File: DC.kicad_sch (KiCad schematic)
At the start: 39 parts, among them U6 MCP2551-I-P, U7 NUCLEO-F302R8

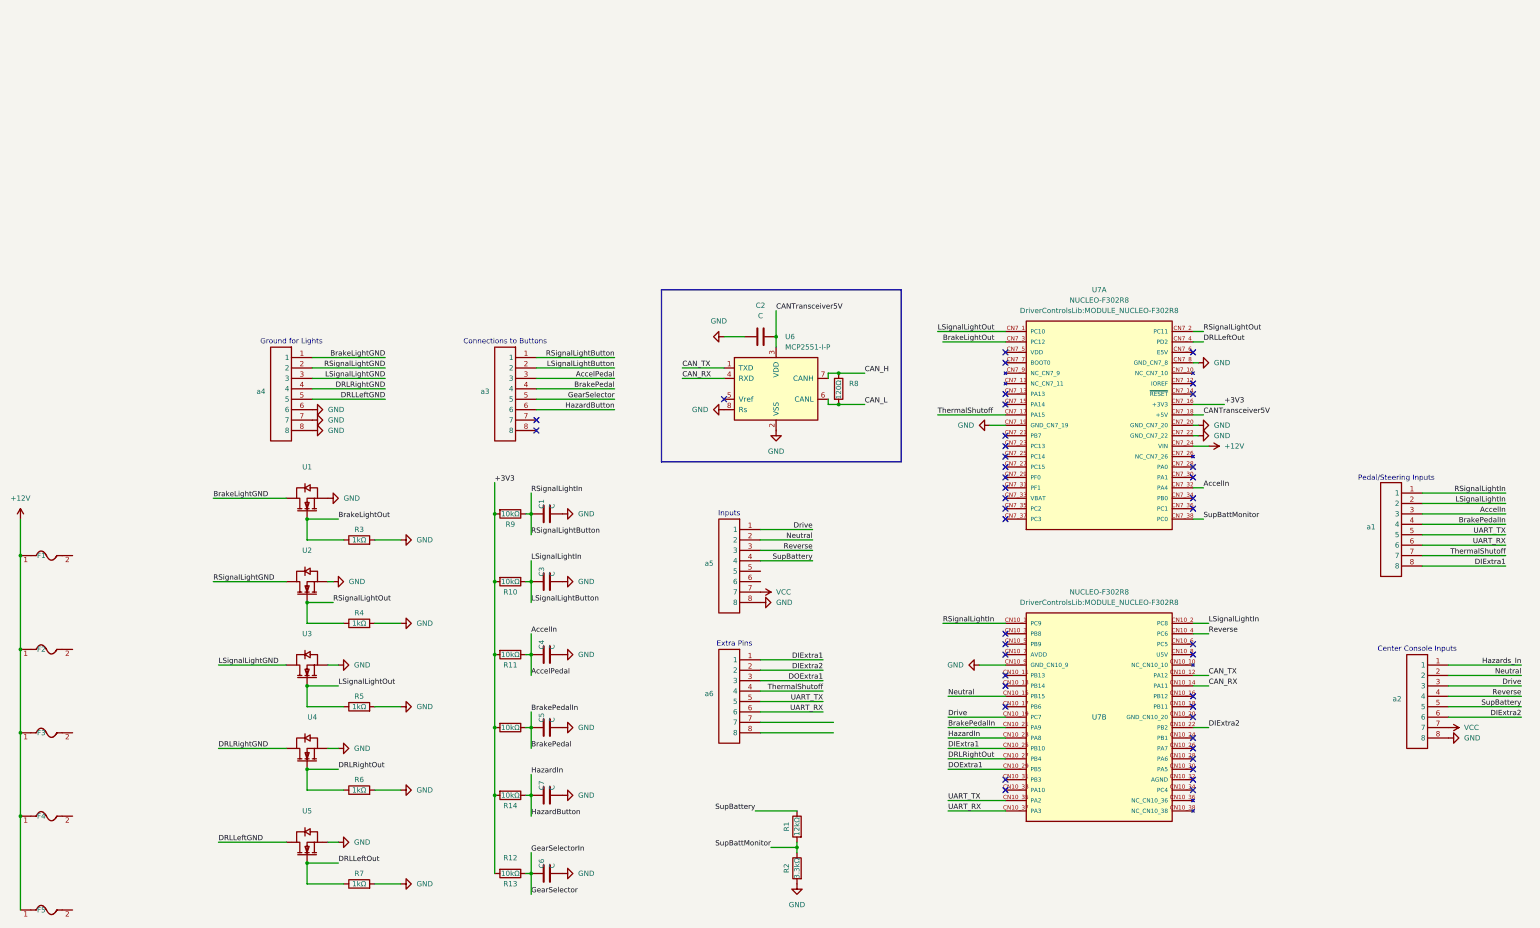
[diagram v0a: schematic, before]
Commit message: added inrush current resistors and fixed gear switch circuit
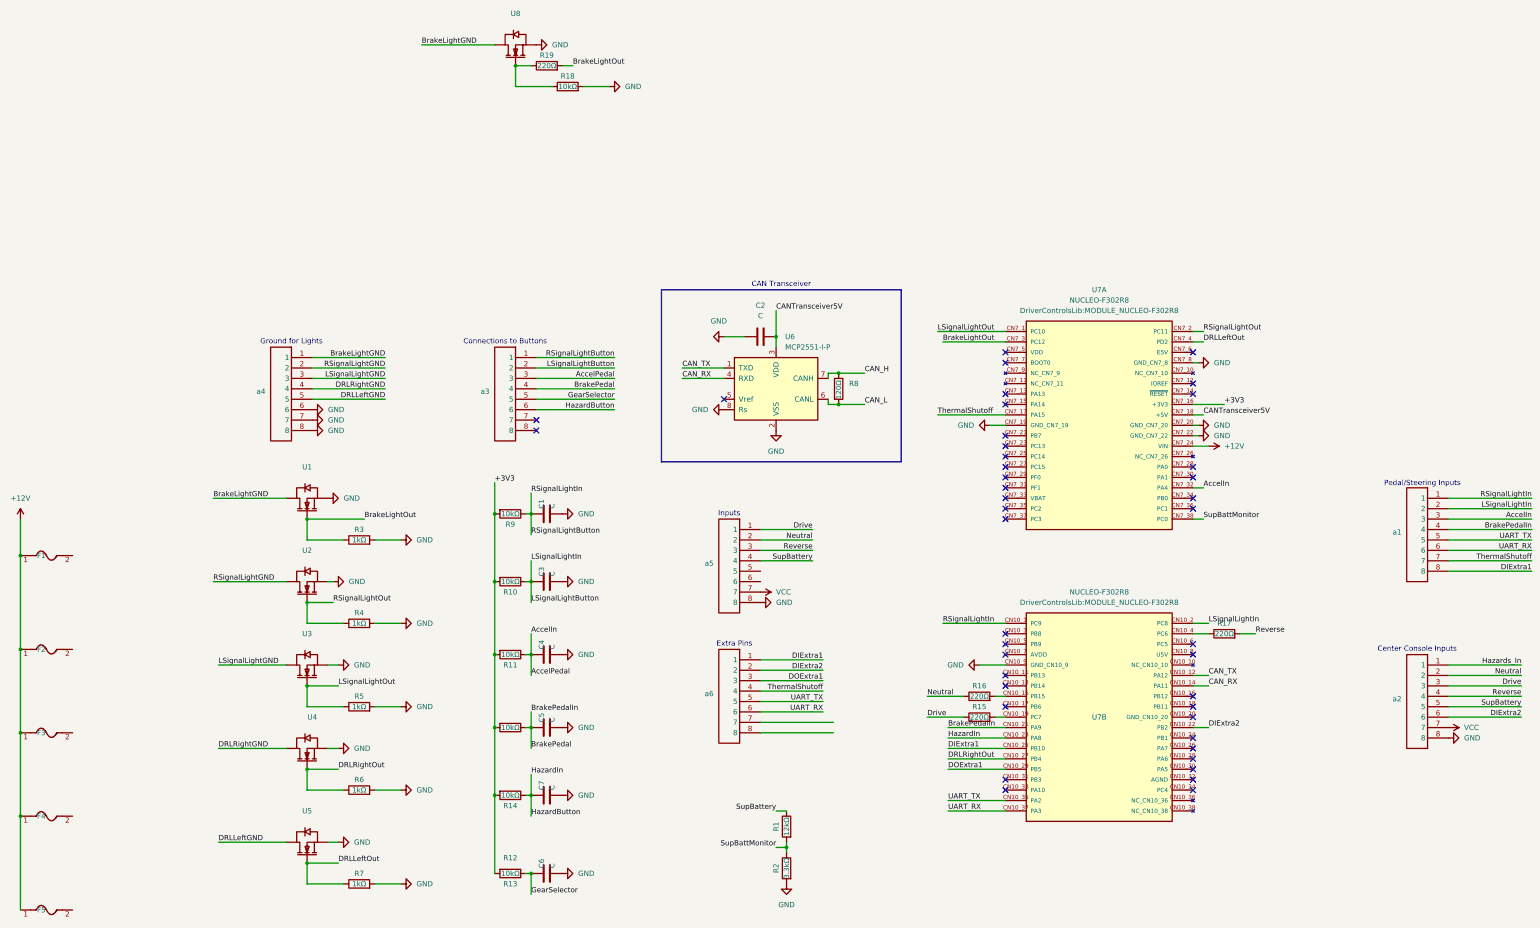
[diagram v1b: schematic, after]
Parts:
- added R15, R16, R17, R19: 220Ω, DriverControlsLib:RES-TH_BD2.2-L6.5-P10.50-D0.6, symbol Device:R
- added R18: 10kΩ, DriverControlsLib:RES-TH_BD2.2-L6.5-P10.50-D0.6, symbol Device:R
- added U8: ~, DriverControlsLib:TO220-3_ONS, symbol DriverControlsLib:FQP30N06L
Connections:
- net BrakeLightGND: now also U8.2 (D)
- net BrakeLightOut: now also R19.2
- net Drive: now also R15.1; no longer U7.CN10_19 (PC7)
- net GND: now also R18.2, U8.3 (S)
- net Neutral: now also R16.1; no longer U7.CN10_15 (PB15)
- net Reverse: now also R17.2; no longer U7.CN10_4 (PC6)
- new net: R17.1, U7.CN10_4 (PC6)
- new net: R15.2, U7.CN10_19 (PC7)
- new net: R16.2, U7.CN10_15 (PB15)
- new net: R18.1, R19.1, U8.1 (G)
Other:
- note added: "CAN Transceiver"
- moved on the sheet: R1, R2, a1

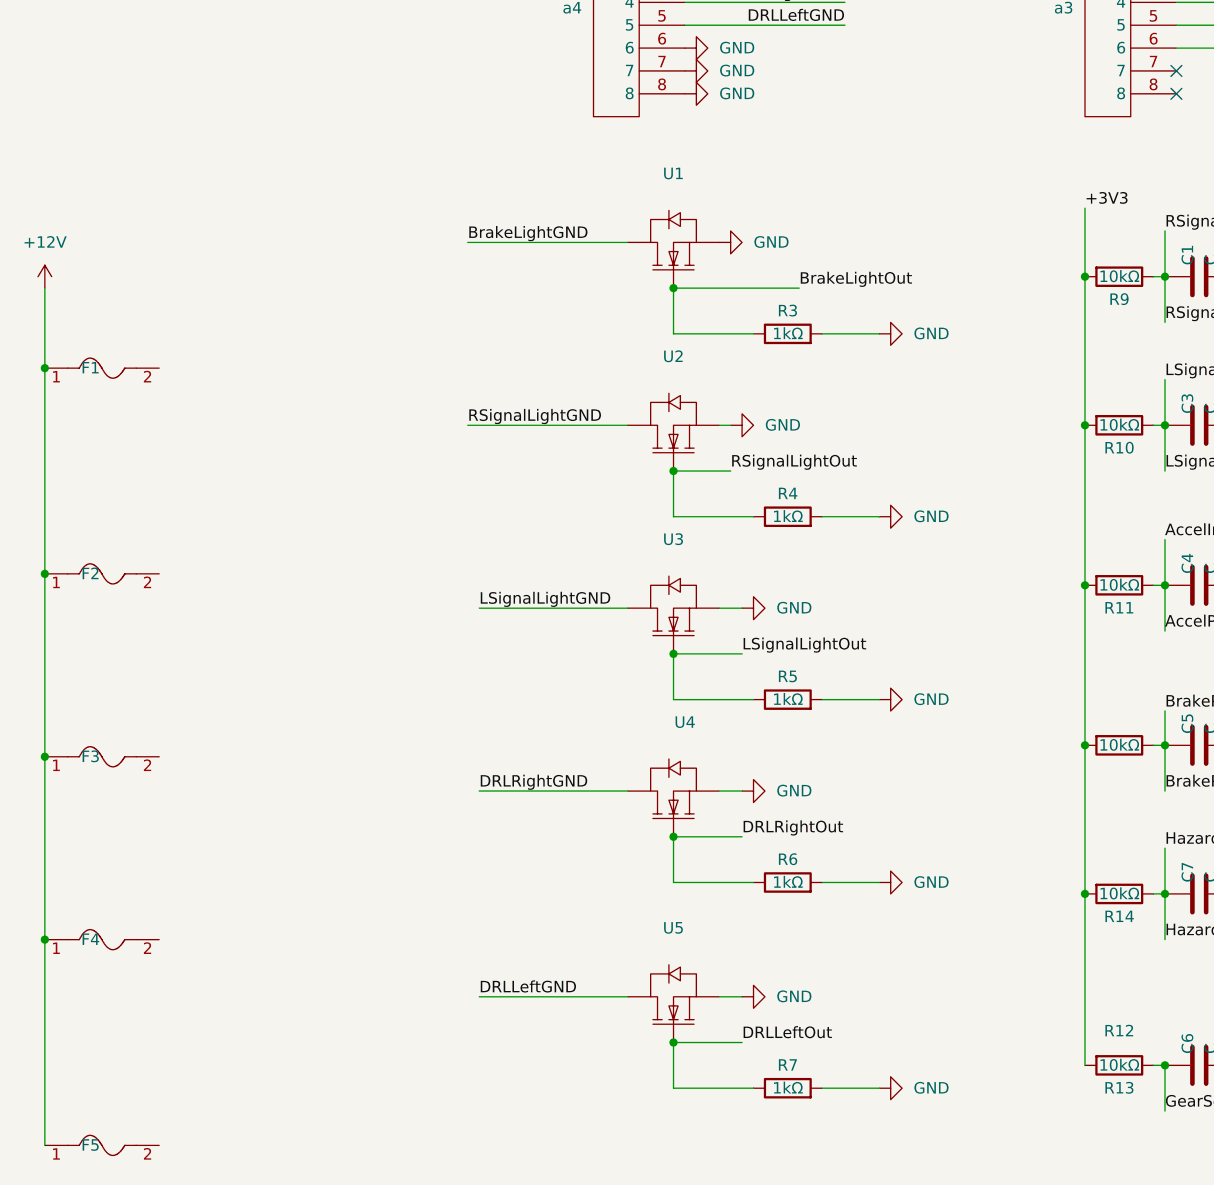
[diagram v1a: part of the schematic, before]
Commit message: changed mosfet circuit
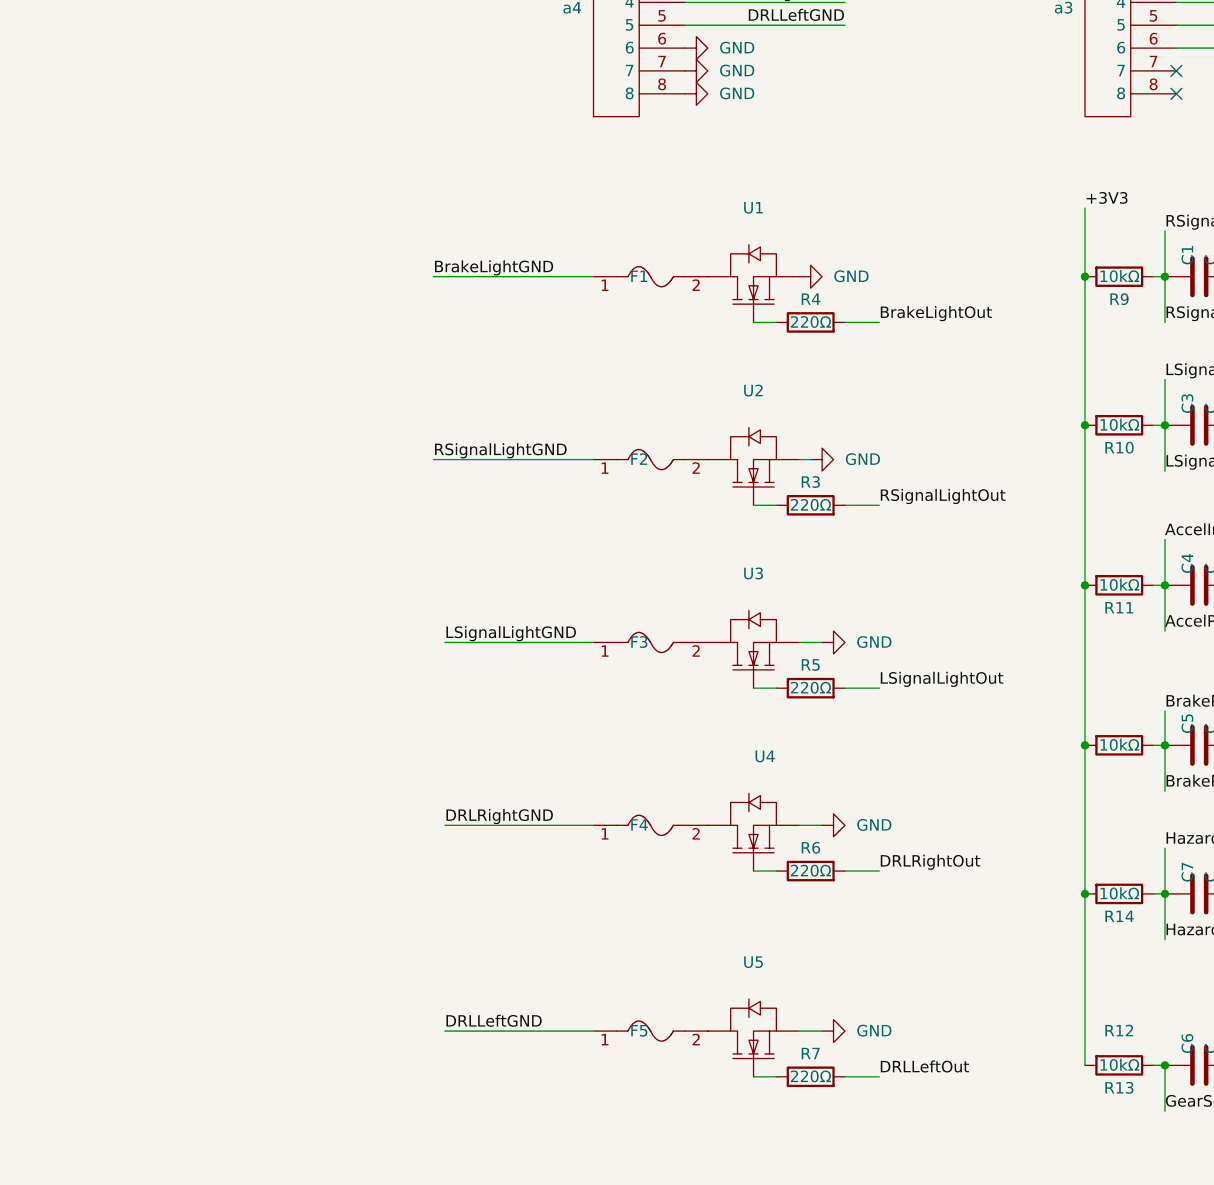
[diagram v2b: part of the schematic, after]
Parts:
- R3, R4, R5, R6, R7: value 1kΩ -> 220Ω
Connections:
- net +12V: no longer F1.1, F2.1, F3.1, F4.1, F5.1
- net BrakeLightGND: now also F1.1; no longer U1.2 (D)
- net BrakeLightOut: now also R4.2; no longer R3.1, U1.1 (G)
- net DRLLeftGND: now also F5.1; no longer U5.2 (D)
- net DRLLeftOut: now also R7.2; no longer R7.1, U5.1 (G)
- net DRLRightGND: now also F4.1; no longer U4.2 (D)
- net DRLRightOut: now also R6.2; no longer R6.1, U4.1 (G)
- net GND: no longer R3.2, R4.2, R5.2, R6.2, R7.2
- net LSignalLightGND: now also F3.1; no longer U3.2 (D)
- net LSignalLightOut: now also R5.2; no longer R5.1, U3.1 (G)
- net RSignalLightGND: now also F2.1; no longer U2.2 (D)
- net RSignalLightOut: now also R3.2; no longer R4.1, U2.1 (G)
- net at F2.2: now also U2.2 (D)
- net at F5.2: now also U5.2 (D)
- net at F4.2: now also U4.2 (D)
- net at F3.2: now also U3.2 (D)
- net at F1.2: now also U1.2 (D)
- new net: R5.1, U3.1 (G)
- new net: R7.1, U5.1 (G)
- new net: R3.1, U2.1 (G)
- new net: R6.1, U4.1 (G)
- new net: R4.1, U1.1 (G)
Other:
- moved on the sheet: F1, F2, F3, F4, F5, U1, U2, U3, U4, U5

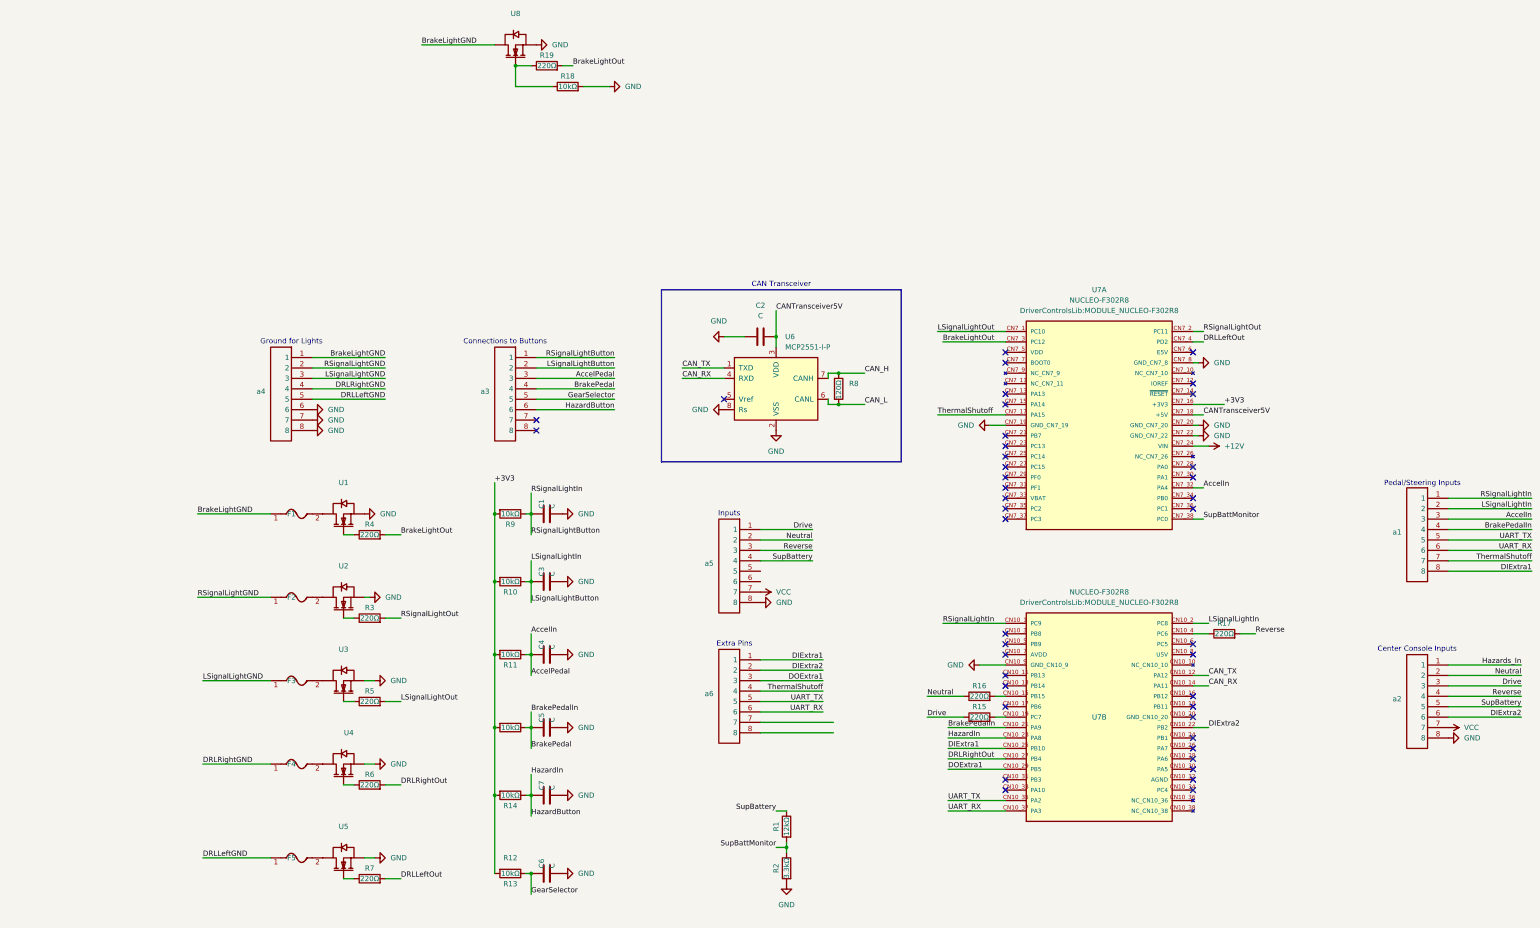
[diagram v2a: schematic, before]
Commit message: fixed the lights mosfets, removed inrush resistors
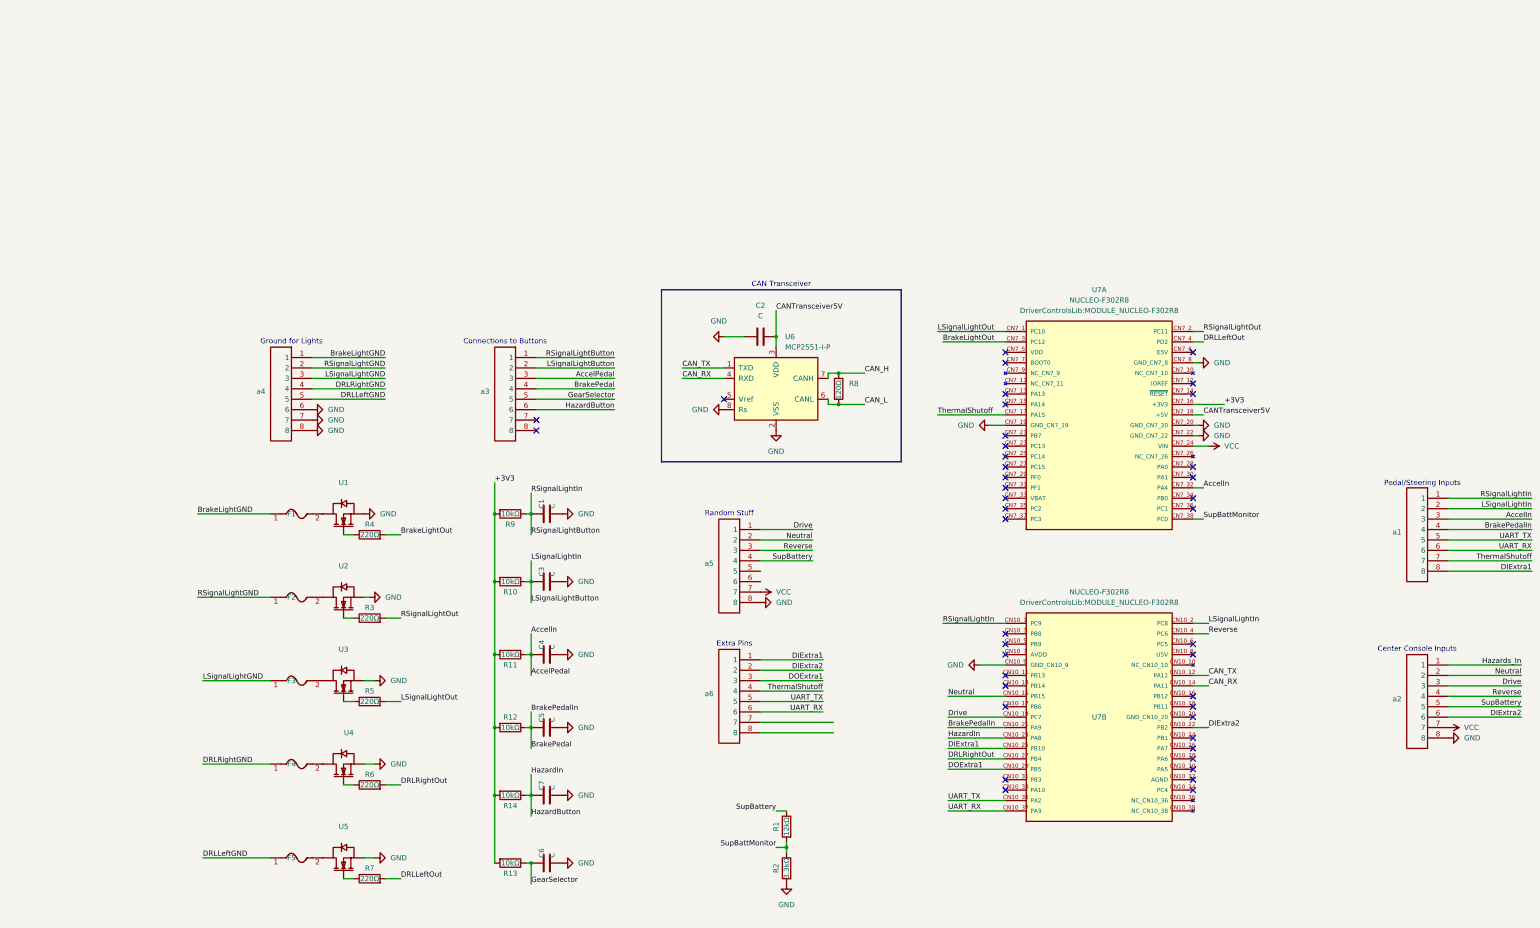
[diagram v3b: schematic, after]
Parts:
- removed R15, R16, R17, R19: 220Ω, DriverControlsLib:RES-TH_BD2.2-L6.5-P10.50-D0.6, symbol Device:R
- removed R18: 10kΩ, DriverControlsLib:RES-TH_BD2.2-L6.5-P10.50-D0.6, symbol Device:R
- removed U8: ~, DriverControlsLib:TO220-3_ONS, symbol DriverControlsLib:FQP30N06L
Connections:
- net +12V is gone; now on net VCC: U7.CN7_24 (VIN)
- net Drive: now also U7.CN10_19 (PC7)
- net Neutral: now also U7.CN10_15 (PB15)
- net Reverse: now also U7.CN10_4 (PC6)
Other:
- note added: "Random Stuff"
- note removed: "Inputs"
- moved on the sheet: C6, R13

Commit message: almost final draft
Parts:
- removed a1, a2: ~, DriverControlsLib:Molex 8 Pin Mini-fit TPA, symbol DriverControlsLib:8 pin connector
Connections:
- net BrakeLightGND renamed BrakeLightNeg
- net DRLLeftGND renamed DRLLeftNeg
- net DRLRightGND renamed DRLRightNeg
- net LSignalLightGND renamed LSignalLightNeg
- net RSignalLightGND renamed RSignalLightNeg
- no-connect marks 42 -> 46
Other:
- note added: ":)"
- note added: "BUTTONS"
- note added: "Gear Selector Inputs and Supplemental Battery"
- note added: "LIGHTS"
- note added: "Negative end of Lights"
- note added: "Supplemental Battery Monitor"
- note removed: "Center Console Inputs"
- note removed: "Ground for Lights"
- note removed: "Pedal/Steering Inputs"
- note removed: "Random Stuff"
- moved on the sheet: C1, C2, C3, C4, C5, C6, C7, R1, R10, R11, R12, R13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

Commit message: pcb tolerances setup, component arrangement
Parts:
- renumbered C3 to C2, C4 to C3, C5 to C4, C7 to C5, C2 to C7, R4 to R1, R14 to R10, R13 to R11, R1 to R12, R2 to R13, R8 to R14, R3 to R2, R5 to R3, R6 to R4, R7 to R5, R9 to R6, R10 to R7, R11 to R8, R12 to R9, a4 to a1, a3 to a2, a5 to a3, a6 to a4
